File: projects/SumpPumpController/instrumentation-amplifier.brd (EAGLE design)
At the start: 22.9 x 14.9 mm, 8 parts, among them CN1 1X4-BIG, U1 AD8293G**ARJZ-R7CT-ND

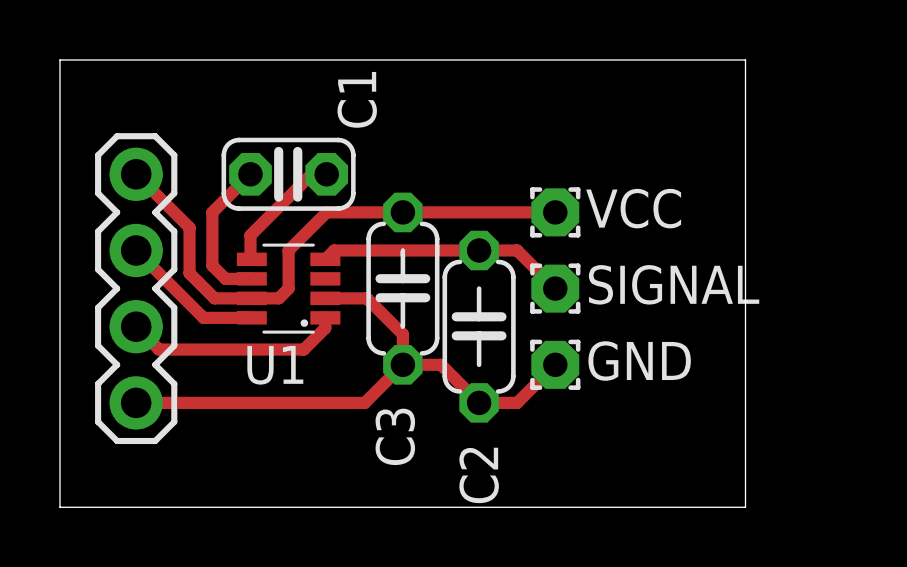
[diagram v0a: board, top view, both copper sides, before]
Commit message: Updated instrumentation schematic to include voltage divider on the reference pin
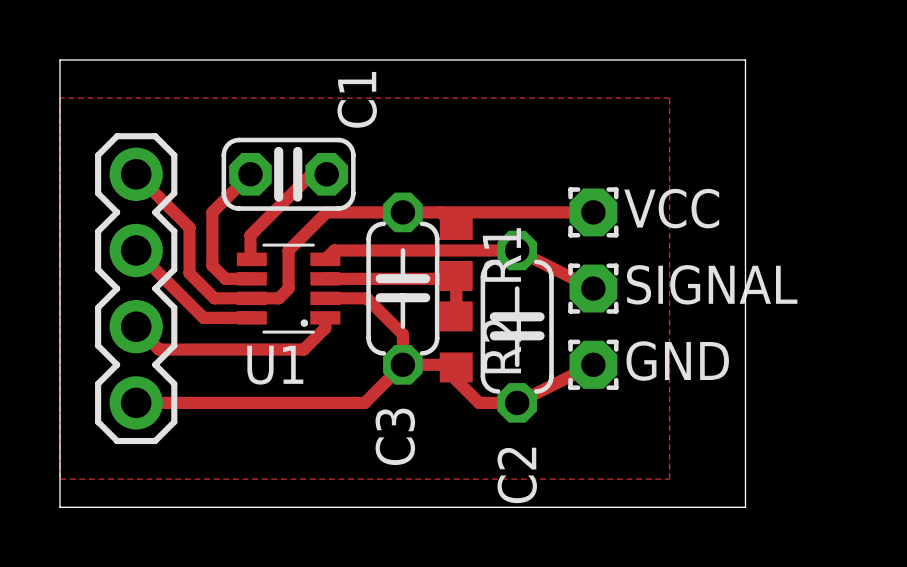
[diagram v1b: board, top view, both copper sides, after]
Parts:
- added R1, R2: 2k, adafruit:R0603
- moved C2 1.27 mm to (15.2, 6.35)
- moved GND 1.27 mm to (17.8, 5.08)
- moved SIGNAL 1.27 mm to (17.8, 7.62)
- moved VCC 1.27 mm to (17.8, 10.2)
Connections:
- new net N$3: R1.2, R2.1, U1.3
- net GND: now also R2.2
- net V+: now also R1.1
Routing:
- net N$3: track 0.00 -> 5.75 mm
- net V+: track 18.5 -> 20.5 mm
- net GND: track 19.6 -> 21.0 mm
- net N$4: track 8.31 -> 9.36 mm
- added copper zone on layer 1, net N$5
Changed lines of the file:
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@@
 </class>
 </classes>
-<designrules name="default">
+<designrules name="default *">
 <description language="de">&lt;b&gt;EAGLE Design Rules&lt;/b&gt;
 &lt;p&gt;
@@
 <param name="mtCopper" value="0.035mm 0.035mm 0.035mm 0.035mm 0.035mm 0.035mm 0.035mm 0.035mm 0.035mm 0.035mm 0.035mm 0.035mm 0.035mm 0.035mm 0.035mm 0.035mm"/>
 <param name="mtIsolate" value="1.5mm 0.15mm 0.2mm 0.15mm 0.2mm 0.15mm 0.2mm 0.15mm 0.2mm 0.15mm 0.2mm 0.15mm 0.2mm 0.15mm 0.2mm"/>
-<param name="mdWireWire" value="8mil"/>
-<param name="mdWirePad" value="8mil"/>
-<param name="mdWireVia" value="8mil"/>
-<param name="mdPadPad" value="8mil"/>
-<param name="mdPadVia" value="8mil"/>
-<param name="mdViaVia" value="8mil"/>
-<param name="mdSmdPad" value="8mil"/>
-<param name="mdSmdVia" value="8mil"/>
-<param name="mdSmdSmd" value="8mil"/>
+<param name="mdWireWire" value="12mil"/>
+<param name="mdWirePad" value="12mil"/>
+<param name="mdWireVia" value="12mil"/>
+<param name="mdPadPad" value="12mil"/>
+<param name="mdPadVia" value="12mil"/>
+<param name="mdViaVia" value="12mil"/>
+<param name="mdSmdPad" value="12mil"/>
+<param name="mdSmdVia" value="12mil"/>
+<param name="mdSmdSmd" value="12mil"/>
 <param name="mdViaViaSameLayer" value="8mil"/>
 <param name="mnLayersViaInSmd" value="2"/>
@@
 <attribute name="VALUE" x="8.382" y="14.097" size="1.27" layer="27" ratio="10" rot="R180"/>
 </element>
-<element name="C2" library="adafruit" package="C050-024X044" value="39nF" x="13.97" y="6.35" smashed="yes" rot="R90">
-<attribute name="NAME" x="14.605" y="0.381" size="1.27" layer="25" ratio="10" rot="R90"/>
-<attribute name="VALUE" x="14.605" y="10.541" size="1.27" layer="27" ratio="10" rot="R90"/>
+<element name="C2" library="adafruit" package="C050-024X044" value="39nF" x="15.24" y="6.35" smashed="yes" rot="R90">
+<attribute name="NAME" x="15.875" y="0.381" size="1.27" layer="25" ratio="10" rot="R90"/>
+<attribute name="VALUE" x="15.875" y="10.541" size="1.27" layer="27" ratio="10" rot="R90"/>
 </element>
 <element name="C3" library="adafruit" package="C050-024X044" value="0.1uF" x="11.43" y="7.62" smashed="yes" rot="R90">
@@
 </element>
 <element name="CN1" library="adafruit" package="1X04-BIG" value="1X4-BIG" x="2.54" y="3.81" smashed="yes" rot="R90"/>
-<element name="VCC" library="wirepad" package="1,6/0,8" value="WIREPAD1,6/0,8" x="16.51" y="10.16" smashed="yes" rot="R270">
-<attribute name="NAME" x="17.526" y="9.652" size="1.27" layer="25" ratio="10"/>
-<attribute name="VALUE" x="17.11" y="10.16" size="0.0254" layer="27" rot="R270"/>
-</element>
-<element name="SIGNAL" library="wirepad" package="1,6/0,8" value="WIREPAD1,6/0,8" x="16.51" y="7.62" smashed="yes" rot="R270">
-<attribute name="NAME" x="17.526" y="7.112" size="1.27" layer="25" ratio="10"/>
-<attribute name="VALUE" x="17.11" y="7.62" size="0.0254" layer="27" rot="R270"/>
-</element>
-<element name="GND" library="wirepad" package="1,6/0,8" value="WIREPAD1,6/0,8" x="16.51" y="5.08" smashed="yes" rot="R270">
-<attribute name="NAME" x="17.526" y="4.572" size="1.27" layer="25" ratio="10"/>
-<attribute name="VALUE" x="17.11" y="5.08" size="0.0254" layer="27" rot="R270"/>
-</element>
+<element name="VCC" library="wirepad" package="1,6/0,8" value="WIREPAD1,6/0,8" x="17.78" y="10.16" smashed="yes" rot="R270">
+<attribute name="NAME" x="18.796" y="9.652" size="1.27" layer="25" ratio="10"/>
+<attribute name="VALUE" x="18.38" y="10.16" size="0.0254" layer="27" rot="R270"/>
+</element>
+<element name="SIGNAL" library="wirepad" package="1,6/0,8" value="WIREPAD1,6/0,8" x="17.78" y="7.62" smashed="yes" rot="R270">
+<attribute name="NAME" x="18.796" y="7.112" size="1.27" layer="25" ratio="10"/>
+<attribute name="VALUE" x="18.38" y="7.62" size="0.0254" layer="27" rot="R270"/>
+</element>
+<element name="GND" library="wirepad" package="1,6/0,8" value="WIREPAD1,6/0,8" x="17.78" y="5.08" smashed="yes" rot="R270">
+<attribute name="NAME" x="18.796" y="4.572" size="1.27" layer="25" ratio="10"/>
+<attribute name="VALUE" x="18.38" y="5.08" size="0.0254" layer="27" rot="R270"/>
+</element>
+<element name="R1" library="adafruit" package="R0603" value="2k" x="13.208" y="8.89" rot="R270"/>
+<element name="R2" library="adafruit" package="R0603" value="2k" x="13.208" y="5.842" rot="R270"/>
 </elements>
 <signals>
@@
 <contactref element="SIGNAL" pad="1"/>
 <wire x1="8.845" y1="8.595" x2="9.14" y2="8.89" width="0.4064" layer="1"/>
-<wire x1="9.14" y1="8.89" x2="13.97" y2="8.89" width="0.4064" layer="1"/>
-<wire x1="16.51" y1="7.62" x2="15.24" y2="8.89" width="0.4064" layer="1"/>
-<wire x1="15.24" y1="8.89" x2="13.97" y2="8.89" width="0.4064" layer="1"/>
+<wire x1="9.14" y1="8.89" x2="15.24" y2="8.89" width="0.4064" layer="1"/>
+<wire x1="17.78" y1="7.62" x2="15.24" y2="8.89" width="0.4064" layer="1"/>
 </signal>
 <signal name="GND">
@@
 <contactref element="CN1" pad="1"/>
 <wire x1="2.54" y1="3.81" x2="10.16" y2="3.81" width="0.4064" layer="1"/>
-<wire x1="16.51" y1="5.08" x2="15.24" y2="3.81" width="0.4064" layer="1"/>
-<wire x1="15.24" y1="3.81" x2="13.97" y2="3.81" width="0.4064" layer="1"/>
-<wire x1="13.97" y1="3.81" x2="12.7" y2="5.08" width="0.4064" layer="1"/>
-<wire x1="12.7" y1="5.08" x2="11.43" y2="5.08" width="0.4064" layer="1"/>
+<wire x1="17.78" y1="5.08" x2="15.24" y2="3.81" width="0.4064" layer="1"/>
 <wire x1="11.43" y1="5.08" x2="10.16" y2="3.81" width="0.4064" layer="1"/>
 <wire x1="8.845" y1="7.295" x2="10.231" y2="7.295" width="0.4064" layer="1"/>
 <wire x1="10.231" y1="7.295" x2="11.43" y2="6.096" width="0.4064" layer="1"/>
 <wire x1="11.43" y1="6.096" x2="11.43" y2="5.08" width="0.4064" layer="1"/>
+<contactref element="R2" pad="2"/>
+<wire x1="11.43" y1="5.08" x2="13.208" y2="5.08" width="0.4064" layer="1"/>
+<wire x1="13.208" y1="5.08" x2="13.208" y2="4.992" width="0.4064" layer="1"/>
+<wire x1="13.208" y1="4.992" x2="13.208" y2="4.572" width="0.4064" layer="1"/>
+<wire x1="13.208" y1="4.572" x2="13.97" y2="3.81" width="0.4064" layer="1"/>
+<wire x1="13.97" y1="3.81" x2="15.24" y2="3.81" width="0.4064" layer="1"/>
 </signal>
 <signal name="V+">
@@
 <contactref element="C3" pad="2"/>
 <contactref element="CN1" pad="4"/>
-<wire x1="16.51" y1="10.16" x2="11.43" y2="10.16" width="0.4064" layer="1"/>
+<wire x1="17.78" y1="10.16" x2="12.7" y2="10.16" width="0.4064" layer="1"/>
+<wire x1="12.7" y1="10.16" x2="11.43" y2="10.16" width="0.4064" layer="1"/>
 <wire x1="2.54" y1="11.43" x2="4.318" y2="9.652" width="0.4064" layer="1"/>
 <wire x1="4.318" y1="9.652" x2="4.318" y2="8.128" width="0.4064" layer="1"/>
@@
 <wire x1="7.62" y1="7.62" x2="7.295" y2="7.295" width="0.4064" layer="1"/>
 <wire x1="7.295" y1="7.295" x2="6.395" y2="7.295" width="0.4064" layer="1"/>
+<contactref element="R1" pad="1"/>
+<wire x1="13.208" y1="9.74" x2="13.12" y2="9.74" width="0.4064" layer="1"/>
+<wire x1="13.12" y1="9.74" x2="12.7" y2="10.16" width="0.4064" layer="1"/>
 </signal>
 <signal name="N$6">
@@
 <wire x1="8.845" y1="6.305" x2="8.845" y2="6.645" width="0.4064" layer="1"/>
 </signal>
+<signal name="N$3">
+<contactref element="R2" pad="1"/>
+<contactref element="R1" pad="2"/>
+<contactref element="U1" pad="3"/>
+<wire x1="13.208" y1="6.692" x2="13.208" y2="8.04" width="0.4064" layer="1"/>
+<wire x1="8.845" y1="7.945" x2="13.113" y2="7.945" width="0.4064" layer="1"/>
+<wire x1="13.113" y1="7.945" x2="13.208" y2="8.04" width="0.4064" layer="1"/>
+</signal>
+<signal name="N$5">
+<polygon width="0.4064" layer="1">
+<vertex x="0" y="13.97"/>
+<vertex x="0" y="1.27"/>
+<vertex x="20.32" y="1.27"/>
+<vertex x="20.32" y="13.97"/>
+</polygon>
+</signal>
 </signals>

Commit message: Added more debug output Adjusted instrumentation amplifier circuit to inlude ~1Hz filter, as turbulence in the sensor triggers false positives; Fixed a bug where self test time was not accounted for when delaying DC pump measurement;
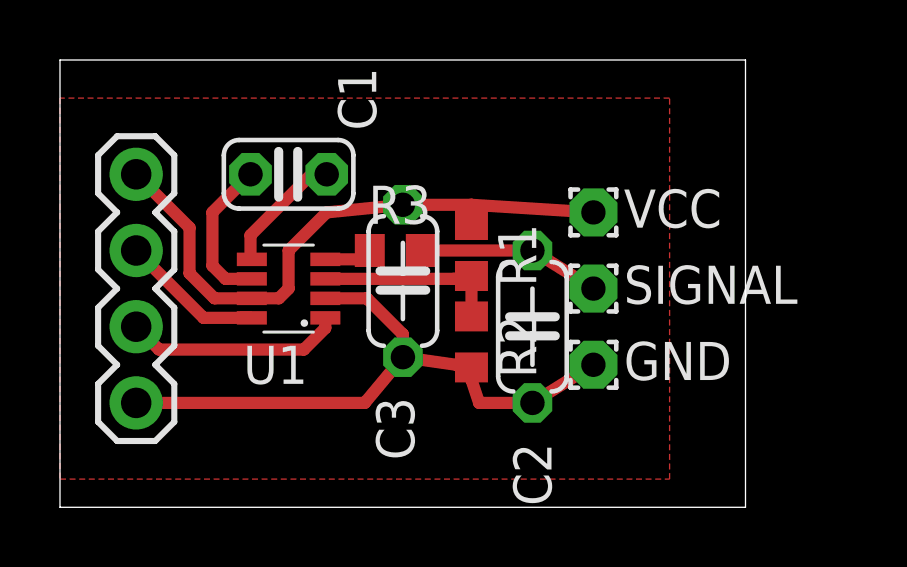
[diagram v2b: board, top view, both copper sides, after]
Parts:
- added R3: 22k, adafruit:R0603
- C2: value 39nF -> 0.47uF
- moved C2 0.51 mm to (15.7, 6.35)
- moved R1 0.51 mm to (13.7, 8.89)
- moved R2 0.51 mm to (13.7, 5.84)
- moved C3 0.25 mm to (11.4, 7.87)
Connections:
- new net N$8: R3.1, U1.4
- net N$4: now also R3.2; no longer U1.4
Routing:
- net N$4: track 9.36 -> 6.12 mm
- net N$8: track 0.00 -> 1.78 mm
